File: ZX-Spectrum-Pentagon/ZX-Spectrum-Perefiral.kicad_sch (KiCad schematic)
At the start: 0 parts

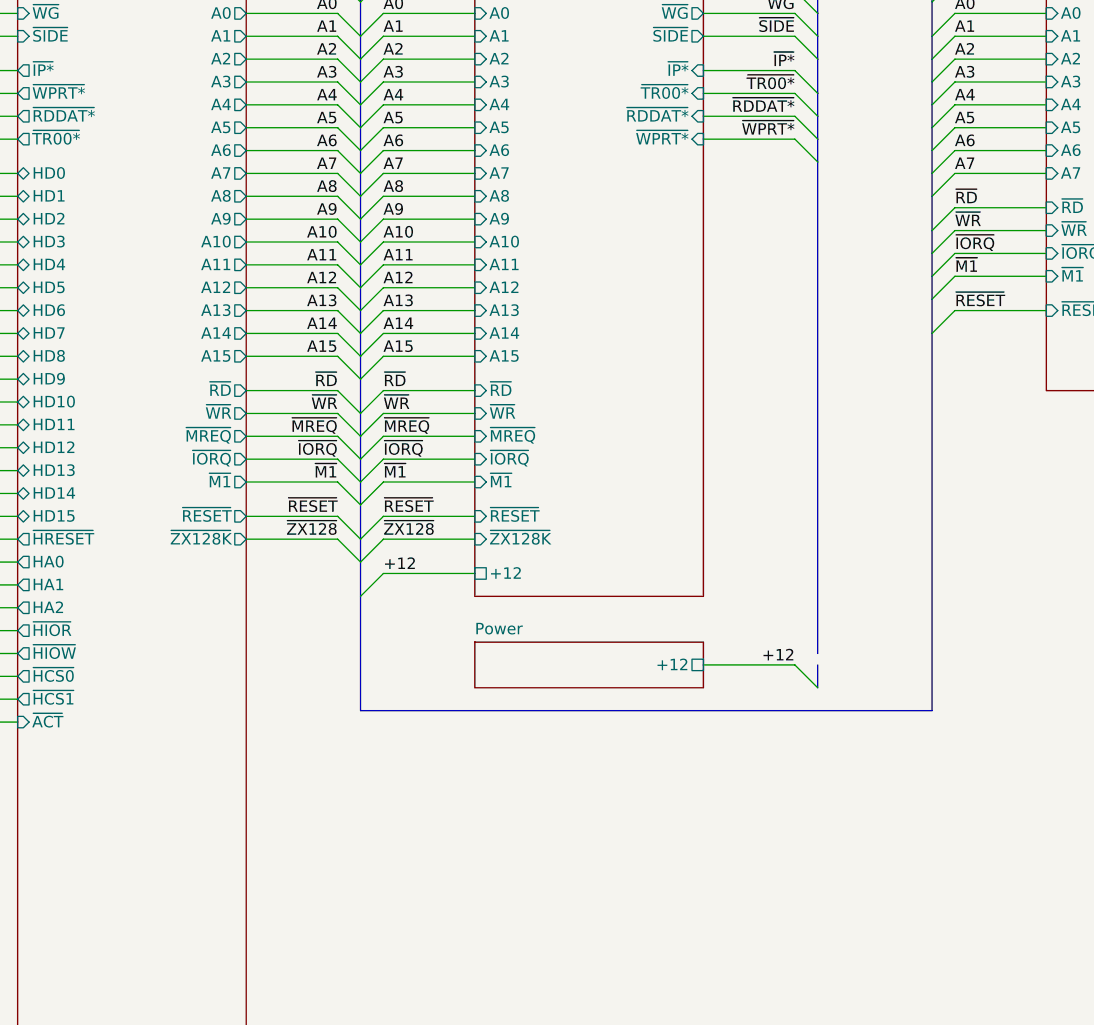
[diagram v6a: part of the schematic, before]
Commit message: FDControlers rename from VCC1 to VDD zx_custom_symbol add connector Conn_02x32_Odd_Even ZX-Spectrum-Pentagon rename from +9V to POWER ZX-Spectrum-Perefiral improve schematic
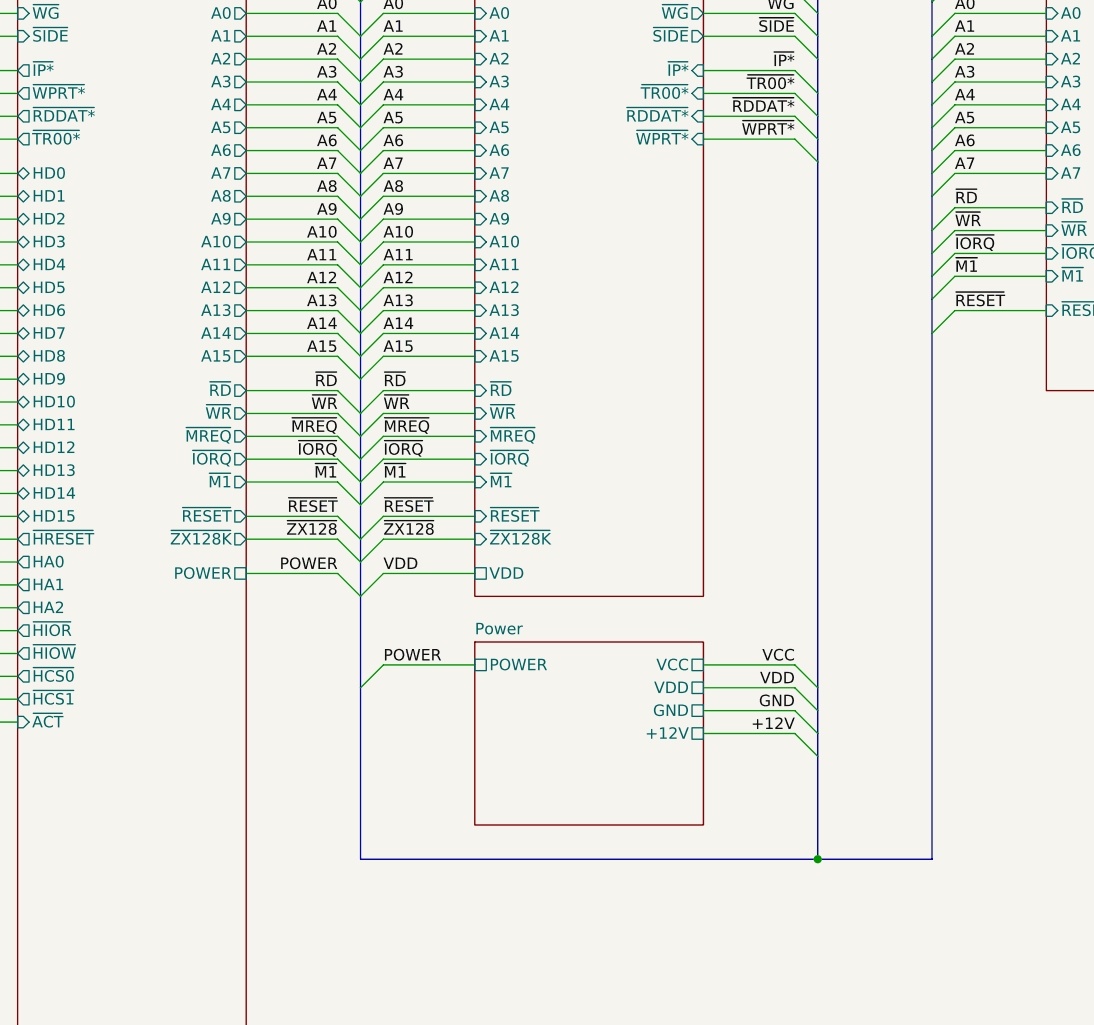
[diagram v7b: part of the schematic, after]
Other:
- sheet Connectors ports: added POWER; removed none
- sheet FDC ports: added VDD; removed +12
- sheet Power ports: added +12V, GND, POWER, VCC, VDD; removed +12
